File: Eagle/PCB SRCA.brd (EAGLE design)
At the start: 160 x 100 mm, 56 parts, among them IC1 DSPIC30F4011-30I_P, IC2 LM324LVIDR, IC3 LMT86QDCKRQ1, IC4 LORA_MOTE, J1 TBL002A-350-03GR-2OR, J2 TBL002A-350-03GR-2OR, J3 TBL002A-350-03GR-2OR, J4 172447-0004, Q1 TIP41C, T1 2N3904, T10 2N3904, T11 2N3904, T2 2N3904, T3 2N3904, T4 2N3904, T5 2N3904, T6 2N3904, T7 2N3904, T8 2N3904, T9 2N3904

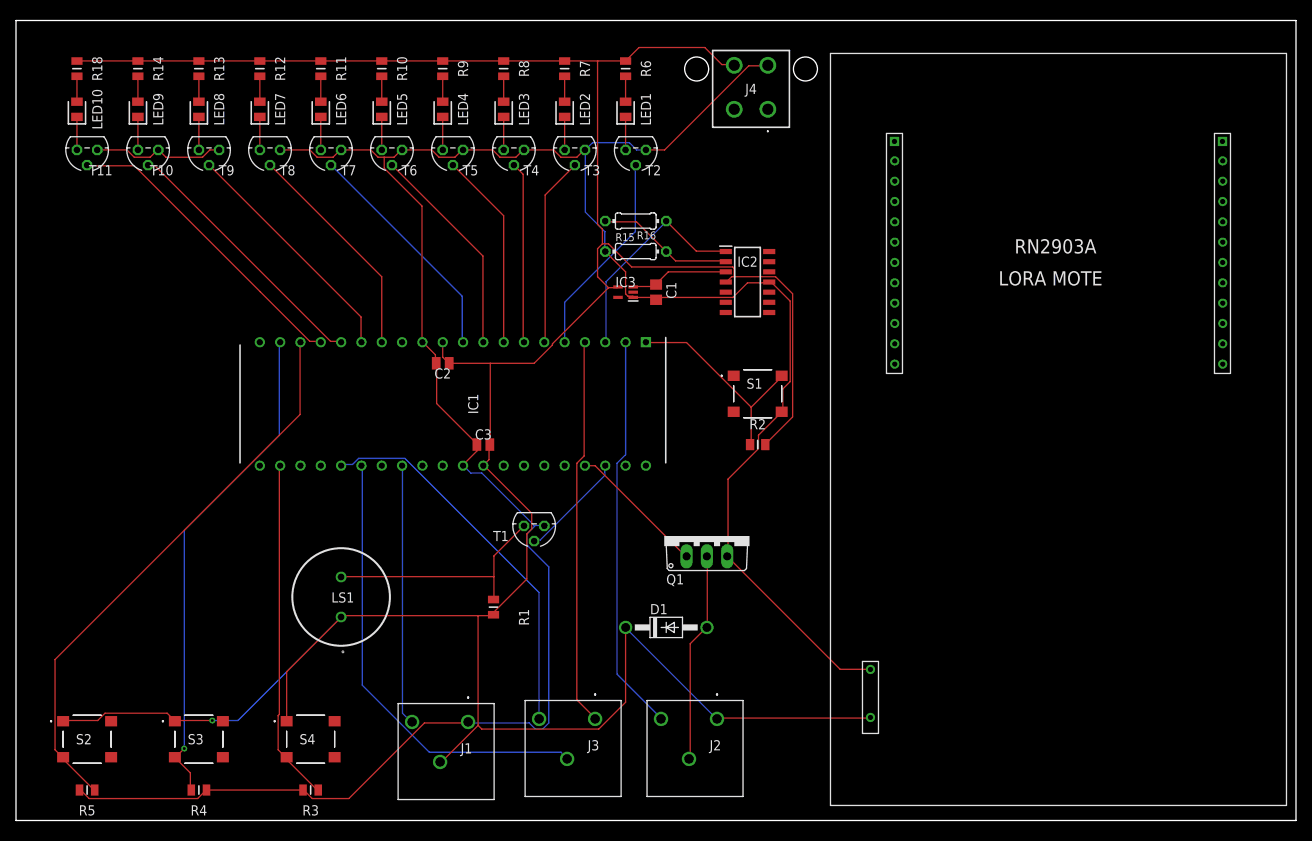
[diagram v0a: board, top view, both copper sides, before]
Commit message: 21/07/2021
cambios en las posiciones de los componentes y pistas
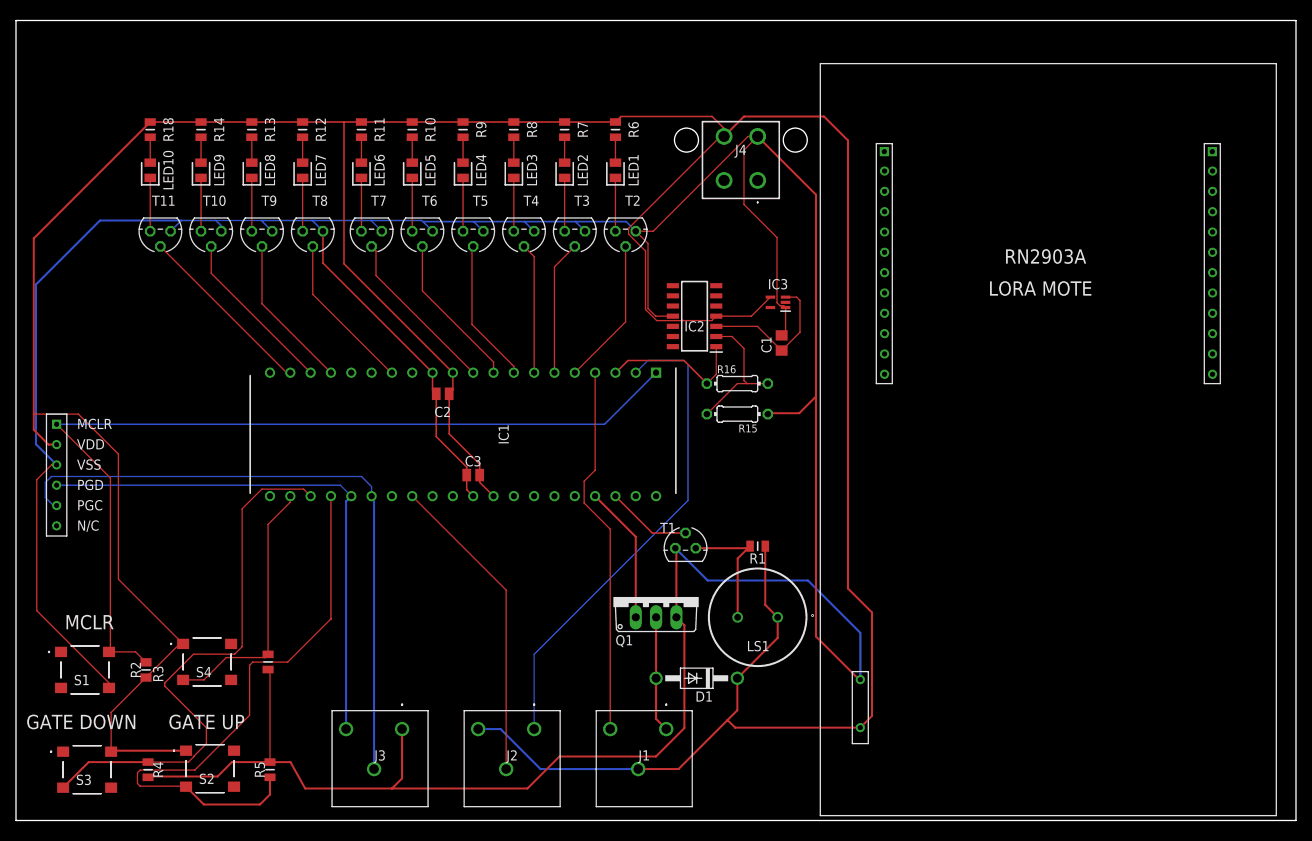
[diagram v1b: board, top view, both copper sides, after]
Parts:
- added J5: ICSP, ICSP:ICSP
- moved S1 90.9 mm to (8.63, 18.8)
- moved R2 81.5 mm to (16.2, 18.8), turned to 270 degrees
- moved LS1 52.1 mm to (92.7, 25.4), turned to 270 degrees
- moved R1 33.9 mm to (92.7, 34.3), turned to 0 degrees
- moved J1 24.8 mm to (81.3, 11.4)
- moved J3 24.2 mm to (48.3, 11.4)
- moved R15 24.0 mm to (90.2, 50.8), turned to 180 degrees
- moved R16 24.0 mm to (90.2, 54.6), turned to 0 degrees
- moved R5 23.0 mm to (31.8, 6.35), turned to 270 degrees
- moved J2 22.9 mm to (64.8, 11.4)
- moved T1 19.1 mm to (83.7, 34.0), turned to 0 degrees
- moved IC3 19.1 mm to (95.2, 64.8)
- moved C1 16.9 mm to (95.7, 59.7), turned to 90 degrees
- moved R3 16.9 mm to (31.5, 19.8), turned to 90 degrees
- moved S4 16.1 mm to (23.9, 19.8)
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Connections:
- net POWER_ERROR renamed L_POWER_ERROR
- net RX_DATA renamed L_RX_DATA
- net SONAR_DATA renamed L_SONAR_DATA
- net TX_DATA renamed L_TX_DATA
- removed net GND1: T10.3, T11.3, T9.3
- new net N$20: S3.A1
- net FAN1: now also J1.A1; no longer J2.B1
- net GATE_DOWN: now also IC1.23; no longer IC1.19
- net GATE_UP: now also IC1.24; no longer IC1.18
- net GND: now also J3.A1, J5.VSS, T10.3, T11.3, T9.3; no longer J1.A1
- net I2C_SCL: now also J5.PGD
- net I2C_SDA: now also J5.PGC
- net LED10: now also IC1.19; no longer IC1.17
- net LED8: now also IC1.17; no longer IC1.15
- net LED9: now also IC1.18; no longer IC1.16
- net MCLR: now also J5.MCLR
- net POT_LINEAR: now also J1.A2; no longer J3.A1
- net RX_UART: now also IC1.16; no longer IC1.30
- net SONAR_ADC: now also J2.A1; no longer J2.A2
- net SONAR_SERIAL: now also J2.B1; no longer J1.A2
- net TX_UART: now also IC1.15; no longer IC1.29
- net V5: now also J2.A2, J5.VDD, S3.B1; no longer J2.A1, S3.A1
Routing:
- net GND: track 320.6 -> 483.9 mm
- net MCLR: track 26.8 -> 114.0 mm
- net V5: track 387.8 -> 459.1 mm, vias 1 -> 0
- net I2C_SDA: track 57.0 -> 81.2 mm
- net I2C_SCL: track 47.9 -> 66.8 mm
- net GND1: track 16.8 -> 0.00 mm
- net LED10: track 38.4 -> 22.8 mm
- net N$3: track 29.9 -> 16.1 mm
- net LED9: track 33.3 -> 20.9 mm
- net FAN1: track 26.3 -> 14.5 mm
- net SONAR_ADC: track 49.8 -> 60.9 mm
- net LED8: track 30.0 -> 19.4 mm
- net AVAILABLE: track 43.1 -> 32.9 mm
- net TEMP: track 27.3 -> 18.4 mm
- net LED7: track 27.9 -> 19.9 mm
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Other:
- board text added: "GATE DOWN"
- board text added: "GATE UP"
- board text added: "MCLR"

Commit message: 22/07/2021
Se actualizo la pcb con todos los componentes y pistas, además se agregó las librerías del proyecto
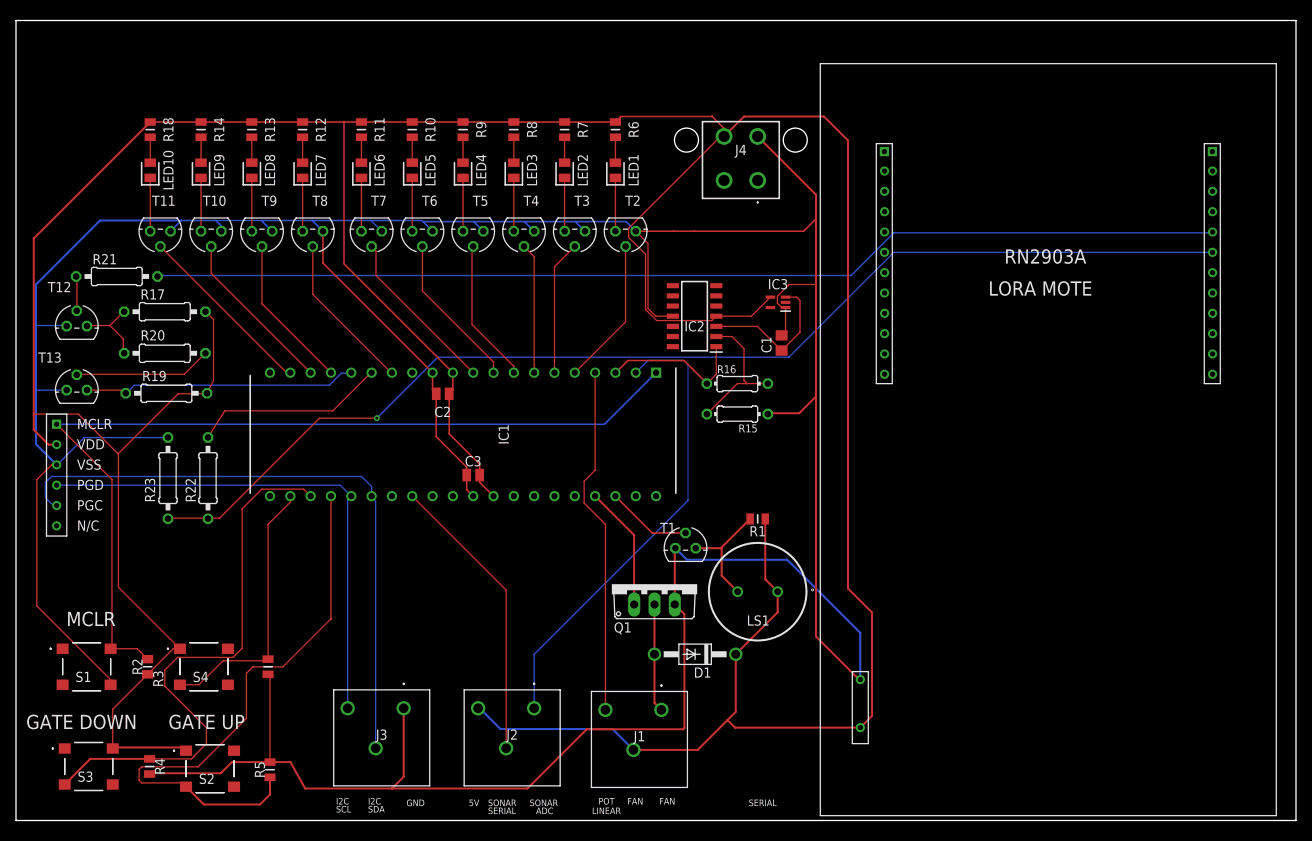
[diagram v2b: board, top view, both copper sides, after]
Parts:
- added R17, R19, R20, R21, R22, R23: (no value), rcl:0207/10
- added T12, T13: 2N3904, transistor-neu-to92:TO92
- moved R1 3.40 mm to (92.7, 37.7)
- moved LS1 3.20 mm to (92.7, 28.6)
- moved D1 3.01 mm to (84.9, 20.8)
- moved J3 2.61 mm to (48.5, 14.0)
- moved J2 2.60 mm to (64.8, 14.0)
- moved J1 2.47 mm to (80.7, 13.8)
- moved Q1 1.61 mm to (79.8, 29.5)
- moved S4 0.72 mm to (23.5, 19.2)
- moved R3 0.60 mm to (31.5, 19.2)
- moved R4 0.45 mm to (16.7, 6.75)
- moved S3 0.45 mm to (9.09, 6.75)
- moved R2 0.45 mm to (16.4, 19.2)
- moved S1 0.45 mm to (8.83, 19.2)
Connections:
- new net N$23: R17.1, R20.2, T12.1
- new net N$24: R21.1, T12.2
- new net N$26: R20.1, T13.2
- net GND: now also R23.1, T12.3, T13.3
- net RX_LORA: now also R22.1, R23.2
- net RX_UART: now also R19.1, T13.1
- net TX_LORA: now also R21.2
- net TX_UART: now also R22.2
- net V5: now also R17.2, R19.2
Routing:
- net RX_LORA: track 0.00 -> 144.4 mm, vias 0 -> 1
- net TX_LORA: track 0.00 -> 134.2 mm
- net RX_UART: track 0.00 -> 34.3 mm
- net V5: track 459.1 -> 486.7 mm
- net TX_UART: track 0.00 -> 24.3 mm
- net N$26: track 0.00 -> 17.2 mm
- net GND: track 483.9 -> 494.4 mm
- net N$23: track 0.00 -> 9.59 mm
- net N$24: track 0.00 -> 4.37 mm
- net I2C_SDA: track 81.2 -> 78.3 mm
- net I2C_SCL: track 66.8 -> 64.1 mm
- net POT_LINEAR: track 46.5 -> 43.8 mm
- net SONAR_SERIAL: track 39.0 -> 36.4 mm
- net SONAR_ADC: track 60.9 -> 58.3 mm
- net FAN: track 17.2 -> 15.6 mm
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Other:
- board text added: "5V"
- board text added: "ADC"
- board text added: "FAN"
- board text added: "GND"
- board text added: "I2C"
- board text added: "LINEAR"
- board text added: "POT"
- board text added: "SCL"
- board text added: "SDA"
- board text added: "SERIAL"
- board text added: "SONAR"
- board text added: "SONAR SERIAL"

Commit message: 11/08/2021
cambios pre finales del pcb y sus componentes
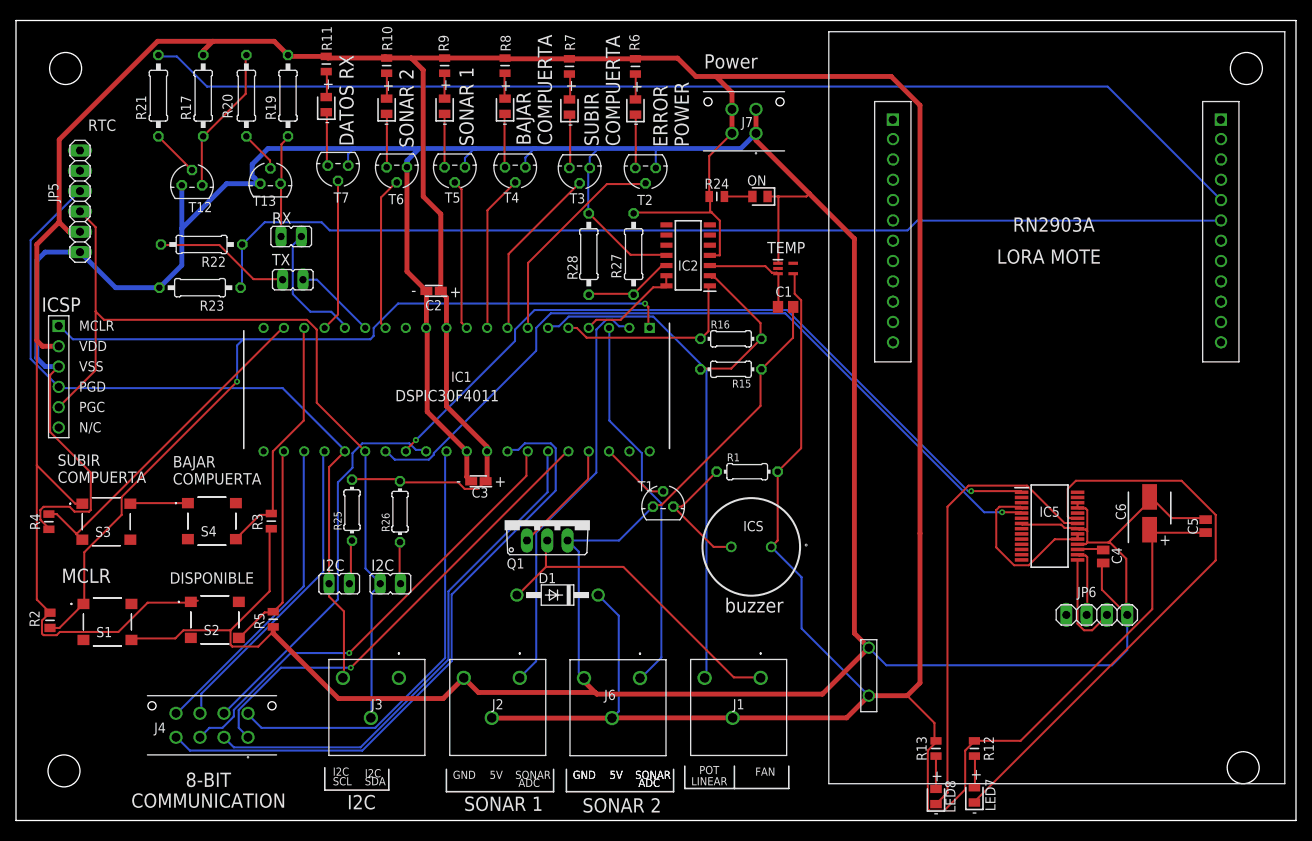
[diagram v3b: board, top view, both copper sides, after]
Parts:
- removed LED10, LED9: 599-0181-007F, 599-0181-007F:LEDC2012X70N
- removed LS1: PS1240P02BT, PS1240P02BT:PS1240P02BT
- removed R14, R18: RC0805FR-071KL, RC0805FR-071KL:RESC2012X60N
- removed T10, T11, T8, T9: 2N3904, transistor-neu-to92:TO92
- added C4, C5: C0805X104K1RAC3316, C0805X104K1RAC3316:CAPC2012X100N
- added C6: UUP1C100MCL1GS, UUP1C100MCL1GS:CAPAE530X610N
- added IC5: FT232RL-REEL, FT232RL-REEL:SOP65P778X200-28N
- added ICS: PS1240P02BT, PS1240P02BT:PS1240P02BT
- added J6: TBL002A-350-03GR-2OR, TBL002A-350-03GR-2OR:TBL002A35003GR2OR
- added J7: 44914-0401, 44914-0401:44914-0401
- added JP1, JP2, JP3, JP4: (no value), jumper:JP1
- added JP5: (no value), pinhead:1X06
- added JP6: (no value), pinhead:1X04
- added ON: 599-0181-007F, 599-0181-007F:LEDC2012X70N
- added R24: RC0805FR-071KL, RC0805FR-071KL:RESC2012X60N
- added R25, R26: (no value), rcl:0204/7
- added R27, R28: (no value), rcl:0207/10
- C2, C3: value C0805X104K1RAC3316 -> TAJR104K020RNJ; device C0805X104K1RAC3316:CAPC2012X100N -> TAJR104K020RNJ:CAPPM2014X120N
- J4: value 172447-0004 -> 44914-0801; device 172447-0004:1724470004 -> 44914-0801:44914-0801
- R1: value RC0805FR-071KL -> (none); device RC0805FR-071KL:RESC2012X60N -> rcl:0204/7
- moved LED8 115.9 mm to (115.0, 3.00)
- moved R13 115.3 mm to (115.0, 9.00)
- moved LED7 114.7 mm to (119.8, 3.20)
- moved R12 114.2 mm to (119.8, 9.00)
- moved J4 94.4 mm to (29.0, 10.4)
- moved R19 40.2 mm to (34.0, 90.6), turned to 90 degrees
- moved T13 35.4 mm to (31.8, 79.6)
- moved R20 33.8 mm to (28.8, 90.6), turned to 90 degrees
- moved R4 33.1 mm to (4.11, 37.4)
- moved S3 30.7 mm to (11.3, 37.4)
- moved R22 29.2 mm to (23.2, 72.0), turned to 180 degrees
- moved R17 27.4 mm to (23.4, 90.6), turned to 90 degrees
- moved R23 24.1 mm to (23.0, 66.6), turned to 0 degrees
- moved R21 23.2 mm to (17.8, 90.6), turned to 90 degrees
- moved T12 22.7 mm to (22.0, 79.4)
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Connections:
- net SONAR_ADC renamed SONAR_ADC1
- removed net LED10: IC1.19, T11.2
- removed net LED7: IC1.14, T8.2
- removed net LED8: IC1.17, T9.2
- removed net LED9: IC1.18, T10.2
- removed net L_SONAR_DATA: IC1.8, T5.2
- removed net L_TX_DATA: IC1.9, T6.2
- removed net N$13 (its old number): LED7.1, T8.1
- removed net N$3 (its old number): LS1.2, R1.1, T1.1
- removed net SONAR_SERIAL: IC1.28, J2.B1
- removed net TX_UART2: IC1.27
- removed net V5: C2.2, C3.2, D1.C, IC1.11, IC1.32, IC2.4, IC3.4, IC4.V5, J1.B1, J2.A2, J4.4, J5.VDD, LS1.1, R1.2, R10.2, R11.2, R12.2, R13.2, R14.2, R17.2, R18.2, R19.2, R2.2, R6.2, R7.2, R8.2, R9.2, S2.A1, S3.B1, S4.A1
- new net BIT_1: IC1.36, J4.1
- new net BIT_2: IC1.35, J4.2
- new net BIT_3: IC1.34, J4.3
- new net BIT_4: IC1.33, J4.4
- new net BIT_5: IC1.30, J4.5
- new net BIT_6: IC1.29, J4.6
- new net BIT_7: IC1.24, J4.7
- new net BIT_8: IC1.23, J4.8
- new net L_SONAR1_DATA: IC1.10, T5.2
- new net L_SONAR2_DATA: IC1.14, T6.2
- new net N$18: IC5.22, LED8.1
- new net N$19: JP6.1
- new net N$27: IC2.12, R27.1, R28.2
- new net N$28: ON.2, R24.1
- new net N$29: JP2.1, R22.2
- new net N$30: JP1.1, R19.1, T13.1
- new net POWER: IC1.4, IC2.13, IC2.14
- new net SONAR_ADC2: IC1.3, J6.A1
- new net TEMP1: JP4.1, R25.1
- new net TEMP2: JP3.2, R26.1
- new net TEMP3: ICS.2, R1.1, T1.1
- new net UART_RX_2: IC1.28, IC5.1
- new net UART_TX_2: IC1.27, IC5.5
- new net V+: C2.1, C3.1, C5.1, C6.1, D1.C, IC1.11, IC1.32, IC2.4, IC3.4, IC4.V5, ICS.1, J1.B1, J2.B1, J5.VDD, J6.B1, J7.2, J7.4, JP5.5, R1.2, R10.2, R11.2, R12.2, R13.2, R17.2, R19.2, R2.2, R24.2, R25.2, R26.2, R27.2, R6.2, R7.2, R8.2, R9.2, S2.A1, S3.A1
- net AVAILABLE: now also R5.2, S2.D1; no longer R3.2, S4.C1
- net GATE_DOWN: now also IC1.19; no longer IC1.23
- net GATE_UP: now also IC1.18, R3.2, S4.D1; no longer IC1.24, R5.2, S2.C1
- net GND: now also C2.2, C3.2, C4.1, C5.2, C6.2, IC5.18, IC5.21, IC5.25, IC5.26, IC5.7, J2.A2, J6.A2, J7.1, J7.3, JP5.6, JP6.4, ON.1, R28.1; no longer C2.1, C3.1, J3.A1, J4.3, T10.3, T11.3, T8.3, T9.3
- net I2C_SCL: now also JP4.2, JP5.3
- net I2C_SDA: now also JP3.1, JP5.4
- net L_GATEDOWN: now also IC1.9; no longer IC1.7
- net L_GATEUP: now also IC1.8; no longer IC1.6
- net L_POWER_ERROR: now also IC1.7; no longer IC1.5
- net L_RX_DATA: now also IC1.17; no longer IC1.10
- net MCLR: now also S1.A1; no longer S1.B1
- net N$1: now also S3.B1, S4.A1; no longer LED10.1, T11.1
- net N$14: now also IC5.19, IC5.20, IC5.4; no longer LED8.1, T9.1
- net N$15: now also IC5.23, LED7.1; no longer LED9.1, T10.1
- net N$20: now also C4.2, IC5.17; no longer S3.A1
- net N$21: now also IC5.16, JP6.2; no longer LED9.2, R14.1
- net N$22: now also IC5.15, JP6.3; no longer LED10.2, R18.1
- net POT_LINEAR: now also IC1.6; no longer IC1.4
- net RX_UART: now also JP1.2; no longer R19.1, T13.1
- net TEMP: now also IC1.5; no longer IC1.3
- net TX_UART: now also JP2.2; no longer R22.2
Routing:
- net V+: track 0.00 -> 608.6 mm
- net V5: track 486.7 -> 0.00 mm
- net GND: track 494.4 -> 598.3 mm
- net UART_TX_2: track 0.00 -> 99.6 mm, vias 0 -> 1
- net UART_RX_2: track 0.00 -> 94.7 mm, vias 0 -> 2
- net BIT_4: track 0.00 -> 78.5 mm
- net N$15: track 6.67 -> 74.2 mm
- net BIT_2: track 0.00 -> 64.3 mm
- net BIT_1: track 0.00 -> 58.5 mm, vias 0 -> 1
- net BIT_3: track 0.00 -> 58.0 mm, vias 0 -> 1
- net N$18: track 0.00 -> 57.2 mm
- net BIT_5: track 0.00 -> 55.1 mm
- net BIT_6: track 0.00 -> 49.4 mm
- net SONAR_ADC2: track 0.00 -> 47.6 mm
- net GATE_UP: track 72.2 -> 31.2 mm
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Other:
- board text added: "+"
- board text added: "-"
- board text added: "32K"
- board text added: "8-BIT"
- board text added: "BAJAR COMPUERTA"
- board text added: "COMMUNICATION"
- board text added: "DATOS RX"
- board text added: "DISPONIBLE"
- board text added: "DSPIC30F4011"
- board text added: "ERROR POWER"
- board text added: "Gnd"
- board text added: "ICSP"
- board text added: "Power"
- board text added: "RTC"
- board text added: "RX"
- board text added: "SONAR 1"
- board text added: "SONAR 2"
- board text added: "SQW"
- board text added: "SUBIR COMPUERTA"
- board text added: "TEMP"
- board text added: "TX"
- board text added: "Vcc"
- board text added: "buzzer"
- board text removed: "GATE DOWN"
- board text removed: "GATE UP"
- board text removed: "SERIAL"
- board text removed: "SONAR SERIAL"

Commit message: 12/08/2021
correccion de sensor de temperatura
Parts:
- turned R4 to 270 degrees
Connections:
- net GND: now also IC3.2
- net V+: now also IC3.5
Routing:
- net GND: track 598.3 -> 597.8 mm
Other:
- board text added: "Power 5V"
- board text removed: "Power"
